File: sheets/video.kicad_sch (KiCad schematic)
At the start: 29 parts, among them U10 74LS273, U11 74LS05, U5 NEO-G0, U6 uPD4364CX-12, U7 uPD4364CX-12, U80 74HC04, U9 74LS273

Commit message: Adding Mouser Part Numbers
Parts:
- C67: Mouser (none) -> 810-FG28C0G1H221JNT0
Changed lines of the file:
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@@
+      (effects (font (size 1.27 1.27)) hide)
+    )
+    (property "Mouser" "" (at 238.506 146.558 0)
       (effects (font (size 1.27 1.27)) hide)
     )
@@
       (effects (font (size 1.27 1.27)) hide)
     )
+    (property "Mouser" "" (at 286.258 74.93 0)
+      (effects (font (size 1.27 1.27)) hide)
+    )
     (pin "1")
     (pin "2")
@@
       (effects (font (size 1.27 1.27)) hide)
     )
+    (property "Mouser" "" (at 286.258 121.158 0)
+      (effects (font (size 1.27 1.27)) hide)
+    )
     (pin "1")
     (pin "2")
@@
       (effects (font (size 1.27 1.27)) hide)
     )
+    (property "Mouser" "" (at 300.482 71.882 0)
+      (effects (font (size 1.27 1.27)) hide)
+    )
     (pin "1")
     (pin "2")
@@
       (effects (font (size 1.27 1.27)) hide)
     )
+    (property "Mouser" "" (at 286.258 50.546 0)
+      (effects (font (size 1.27 1.27)) hide)
+    )
     (pin "1")
     (pin "2")
@@
       (effects (font (size 1.27 1.27)) hide)
     )
+    (property "Mouser" "" (at 286.258 161.29 0)
+      (effects (font (size 1.27 1.27)) hide)
+    )
     (pin "1")
     (pin "2")
@@
     )
     (property "Datasheet" "" (at 282.194 177.038 0)
+      (effects (font (size 1.27 1.27)) hide)
+    )
+    (property "Mouser" "" (at 282.194 177.038 0)
       (effects (font (size 1.27 1.27)) hide)
     )
@@
       (effects (font (size 1.27 1.27)) hide)
     )
+    (property "Mouser" "" (at 293.37 82.042 0)
+      (effects (font (size 1.27 1.27)) hide)
+    )
     (pin "1")
     (pin "2")
@@
     )
     (property "Datasheet" "" (at 93.726 202.184 0)
+      (effects (font (size 1.27 1.27)) hide)
+    )
+    (property "Mouser" "" (at 93.726 202.184 0)
       (effects (font (size 1.27 1.27)) hide)
     )
@@
       (effects (font (size 1.27 1.27)) hide)
     )
+    (property "Mouser" "" (at 238.506 73.914 0)
+      (effects (font (size 1.27 1.27)) hide)
+    )
     (pin "1")
     (pin "10")
@@
       (effects (font (size 1.27 1.27)) hide)
     )
+    (property "Mouser" "" (at 286.258 62.738 0)
+      (effects (font (size 1.27 1.27)) hide)
+    )
     (pin "1")
     (pin "2")
@@
       (effects (font (size 1.27 1.27)) hide)
     )
+    (property "Mouser" "" (at 300.482 118.11 0)
+      (effects (font (size 1.27 1.27)) hide)
+    )
     (pin "1")
     (pin "2")
@@
       (effects (font (size 1.27 1.27)) hide)
     )
+    (property "Mouser" "" (at 286.258 143.002 0)
+      (effects (font (size 1.27 1.27)) hide)
+    )
     (pin "1")
     (pin "2")
@@
     )
     (property "Datasheet" "" (at 286.258 149.098 0)
+      (effects (font (size 1.27 1.27)) hide)
+    )
+    (property "Mouser" "" (at 286.258 149.098 0)
       (effects (font (size 1.27 1.27)) hide)
     )
@@
       (effects (font (size 1.27 1.27)) hide)
     )
+    (property "Mouser" "" (at 293.37 128.27 0)
+      (effects (font (size 1.27 1.27)) hide)
+    )
     (pin "1")
     (pin "2")
@@
     )
     (property "Datasheet" "" (at 177.038 120.65 0)
+      (effects (font (size 1.27 1.27)) hide)
+    )
+    (property "Mouser" "" (at 177.038 120.65 0)
       (effects (font (size 1.27 1.27)) hide)
     )
@@
     )
     (property "Datasheet" "" (at 139.7 214.884 0)
+      (effects (font (size 1.27 1.27)) hide)
+    )
+    (property "Mouser" "" (at 139.7 214.884 0)
       (effects (font (size 1.27 1.27)) hide)
     )
@@
       (effects (font (size 1.27 1.27)) hide)
     )
+    (property "Mouser" "" (at 177.038 66.294 0)
+      (effects (font (size 1.27 1.27)) hide)
+    )
     (pin "1")
     (pin "10")
@@
       (effects (font (size 1.27 1.27)) hide)
     )
+    (property "Mouser" "" (at 293.37 174.498 0)
+      (effects (font (size 1.27 1.27)) hide)
+    )
     (pin "1")
     (pin "2")
@@
     )
     (property "Datasheet" "" (at 286.258 96.774 0)
+      (effects (font (size 1.27 1.27)) hide)
+    )
+    (property "Mouser" "" (at 286.258 96.774 0)
       (effects (font (size 1.27 1.27)) hide)
     )
@@
       (effects (font (size 1.27 1.27)) hide)
     )
+    (property "Mouser" "810-FG28C0G1H221JNT0" (at 141.478 130.81 0)
+      (effects (font (size 1.27 1.27)) hide)
+    )
     (pin "1")
     (pin "2")
@@
     )
     (property "Datasheet" "" (at 259.842 213.36 0)
+      (effects (font (size 1.27 1.27)) hide)
+    )
+    (property "Mouser" "" (at 259.842 213.36 0)
       (effects (font (size 1.27 1.27)) hide)
     )
@@
       (effects (font (size 1.27 1.27)) hide)
     )
+    (property "Mouser" "" (at 286.258 115.062 0)
+      (effects (font (size 1.27 1.27)) hide)
+    )
     (pin "1")
     (pin "2")
@@
       (effects (font (size 1.27 1.27)) hide)
     )
+    (property "Mouser" "" (at 300.482 164.338 0)
+      (effects (font (size 1.27 1.27)) hide)
+    )
     (pin "1")
     (pin "2")
@@
     )
     (property "Datasheet" "" (at 286.258 167.386 0)
+      (effects (font (size 1.27 1.27)) hide)
+    )
+    (property "Mouser" "" (at 286.258 167.386 0)
       (effects (font (size 1.27 1.27)) hide)
     )
@@
     )
     (property "Datasheet" "" (at 69.342 202.184 0)
+      (effects (font (size 1.27 1.27)) hide)
+    )
+    (property "Mouser" "" (at 69.342 202.184 0)
       (effects (font (size 1.27 1.27)) hide)
     )
@@
       (effects (font (size 1.27 1.27)) hide)
     )
+    (property "Mouser" "" (at 282.194 130.81 0)
+      (effects (font (size 1.27 1.27)) hide)
+    )
     (pin "1")
     (pin "2")
@@
       (effects (font (size 1.27 1.27)) hide)
     )
+    (property "Mouser" "" (at 286.258 102.87 0)
+      (effects (font (size 1.27 1.27)) hide)
+    )
     (pin "1")
     (pin "2")
@@
     )
     (property "Datasheet" "" (at 272.796 83.312 0)
+      (effects (font (size 1.27 1.27)) hide)
+    )
+    (property "Mouser" "" (at 272.796 83.312 0)
       (effects (font (size 1.27 1.27)) hide)
     )
@@
       (effects (font (size 1.27 1.27)) hide)
     )
+    (property "Mouser" "" (at 286.258 68.834 0)
+      (effects (font (size 1.27 1.27)) hide)
+    )
     (pin "1")
     (pin "2")
@@
     )
     (property "Datasheet" "" (at 259.842 227.076 0)
+      (effects (font (size 1.27 1.27)) hide)
+    )
+    (property "Mouser" "" (at 259.842 227.076 0)
       (effects (font (size 1.27 1.27)) hide)
     )
@@
       (effects (font (size 1.27 1.27)) hide)
     )
+    (property "Mouser" "" (at 286.258 155.194 0)
+      (effects (font (size 1.27 1.27)) hide)
+    )
     (pin "1")
     (pin "2")
@@
       (effects (font (size 1.27 1.27)) hide)
     )
+    (property "Mouser" "" (at 286.258 56.642 0)
+      (effects (font (size 1.27 1.27)) hide)
+    )
     (pin "1")
     (pin "2")
@@
       (effects (font (size 1.27 1.27)) hide)
     )
+    (property "Mouser" "" (at 286.258 108.966 0)
+      (effects (font (size 1.27 1.27)) hide)
+    )
     (pin "1")
     (pin "2")
@@
       (effects (font (size 1.27 1.27)) hide)
     )
+    (property "Mouser" "" (at 259.842 199.644 0)
+      (effects (font (size 1.27 1.27)) hide)
+    )

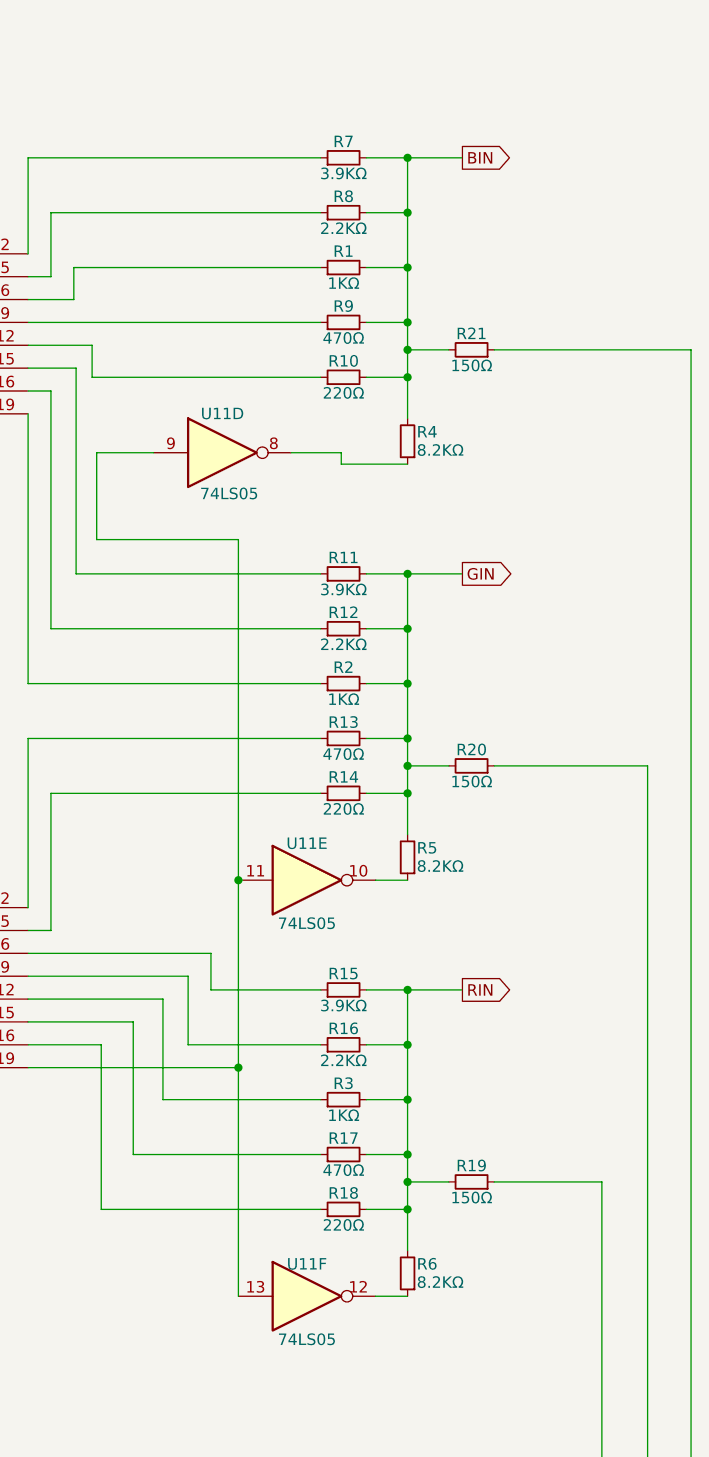
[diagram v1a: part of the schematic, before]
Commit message: More silkscreen tidy up, adding mouser components to BOM
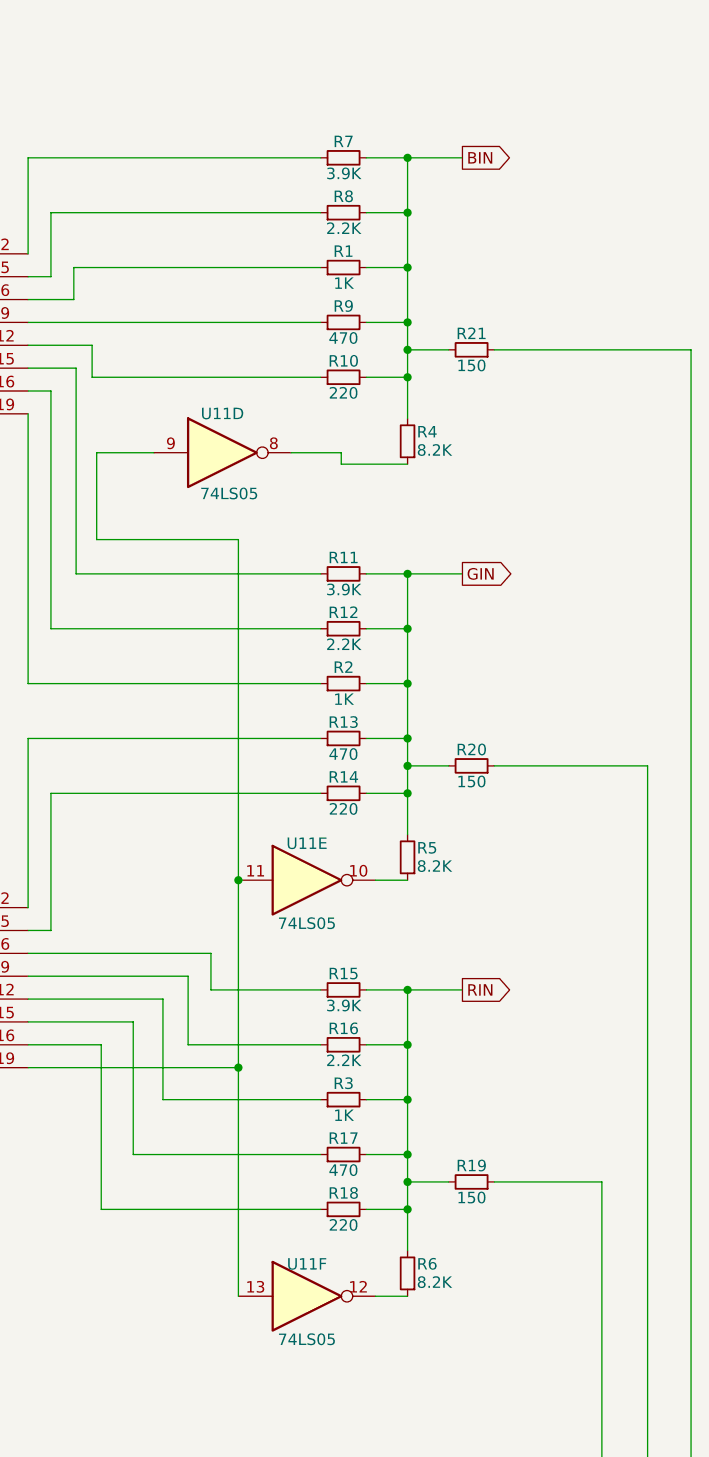
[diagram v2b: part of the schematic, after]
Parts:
- R1, R2, R3: value 1KΩ -> 1K
- R10, R14, R18: value 220Ω -> 220
- R11, R15, R7: value 3.9KΩ -> 3.9K
- R12, R16, R8: value 2.2KΩ -> 2.2K
- R13, R17, R9: value 470Ω -> 470
- R19, R20, R21: value 150Ω -> 150
- R4, R5, R6: value 8.2KΩ -> 8.2K
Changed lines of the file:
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@@
       (effects (font (size 1.27 1.27)))
     )
-    (property "Value" "220Ω" (at 286.258 76.708 90)
+    (property "Value" "220" (at 286.258 76.708 90)
       (effects (font (size 1.27 1.27)))
     )
@@
       (effects (font (size 1.27 1.27)))
     )
-    (property "Value" "220Ω" (at 286.258 122.936 90)
+    (property "Value" "220" (at 286.258 122.936 90)
       (effects (font (size 1.27 1.27)))
     )
@@
       (effects (font (size 1.27 1.27)))
     )
-    (property "Value" "150Ω" (at 300.482 73.66 90)
+    (property "Value" "150" (at 300.482 73.66 90)
       (effects (font (size 1.27 1.27)))
     )
@@
       (effects (font (size 1.27 1.27)))
     )
-    (property "Value" "3.9KΩ" (at 286.258 52.324 90)
+    (property "Value" "3.9K" (at 286.258 52.324 90)
       (effects (font (size 1.27 1.27)))
     )
@@
       (effects (font (size 1.27 1.27)))
     )
-    (property "Value" "470Ω" (at 286.258 163.068 90)
+    (property "Value" "470" (at 286.258 163.068 90)
       (effects (font (size 1.27 1.27)))
     )
@@
       (effects (font (size 1.27 1.27)) (justify right))
     )
-    (property "Value" "8.2KΩ" (at 294.386 83.058 0)
+    (property "Value" "8.2K" (at 294.386 83.058 0)
       (effects (font (size 1.27 1.27)) (justify right))
     )
@@
       (effects (font (size 1.27 1.27)))
     )
-    (property "Value" "1KΩ" (at 286.258 64.516 90)
+    (property "Value" "1K" (at 286.258 64.516 90)
       (effects (font (size 1.27 1.27)))
     )
@@
       (effects (font (size 1.27 1.27)))
     )
-    (property "Value" "150Ω" (at 300.482 119.888 90)
+    (property "Value" "150" (at 300.482 119.888 90)
       (effects (font (size 1.27 1.27)))
     )
@@
       (effects (font (size 1.27 1.27)))
     )
-    (property "Value" "3.9KΩ" (at 286.258 144.78 90)
+    (property "Value" "3.9K" (at 286.258 144.78 90)
       (effects (font (size 1.27 1.27)))
     )
@@
       (effects (font (size 1.27 1.27)))
     )
-    (property "Value" "2.2KΩ" (at 286.258 150.876 90)
+    (property "Value" "2.2K" (at 286.258 150.876 90)
       (effects (font (size 1.27 1.27)))
     )
@@
       (effects (font (size 1.27 1.27)) (justify right))
     )
-    (property "Value" "8.2KΩ" (at 294.386 129.286 0)
+    (property "Value" "8.2K" (at 294.386 129.286 0)
       (effects (font (size 1.27 1.27)) (justify right))
     )
@@
       (effects (font (size 1.27 1.27)) (justify right))
     )
-    (property "Value" "8.2KΩ" (at 294.386 175.514 0)
+    (property "Value" "8.2K" (at 294.386 175.514 0)
       (effects (font (size 1.27 1.27)) (justify right))
     )
@@
       (effects (font (size 1.27 1.27)))
     )
-    (property "Value" "3.9KΩ" (at 286.258 98.552 90)
+    (property "Value" "3.9K" (at 286.258 98.552 90)
       (effects (font (size 1.27 1.27)))
     )
@@
       (effects (font (size 1.27 1.27)))
     )
-    (property "Value" "470Ω" (at 286.258 116.84 90)
+    (property "Value" "470" (at 286.258 116.84 90)
       (effects (font (size 1.27 1.27)))
     )
@@
       (effects (font (size 1.27 1.27)))
     )
-    (property "Value" "150Ω" (at 300.482 166.116 90)
+    (property "Value" "150" (at 300.482 166.116 90)
       (effects (font (size 1.27 1.27)))
     )
@@
       (effects (font (size 1.27 1.27)))
     )
-    (property "Value" "220Ω" (at 286.258 169.164 90)
+    (property "Value" "220" (at 286.258 169.164 90)
       (effects (font (size 1.27 1.27)))
     )
@@
       (effects (font (size 1.27 1.27)))
     )
-    (property "Value" "2.2KΩ" (at 286.258 104.648 90)
+    (property "Value" "2.2K" (at 286.258 104.648 90)
       (effects (font (size 1.27 1.27)))
     )
@@
       (effects (font (size 1.27 1.27)))
     )
-    (property "Value" "470Ω" (at 286.258 70.612 90)
+    (property "Value" "470" (at 286.258 70.612 90)
       (effects (font (size 1.27 1.27)))
     )
@@
       (effects (font (size 1.27 1.27)))
     )
-    (property "Value" "1KΩ" (at 286.258 156.972 90)
+    (property "Value" "1K" (at 286.258 156.972 90)
       (effects (font (size 1.27 1.27)))
     )
@@
       (effects (font (size 1.27 1.27)))
     )
-    (property "Value" "2.2KΩ" (at 286.258 58.42 90)
+    (property "Value" "2.2K" (at 286.258 58.42 90)
       (effects (font (size 1.27 1.27)))
     )
@@
       (effects (font (size 1.27 1.27)))
     )
-    (property "Value" "1KΩ" (at 286.258 110.744 90)
-      (effects (font (size 1.27 1.27)))
-    )
+    (property "Value" "1K" (at 286.258 110.744 90)
+      (effects (font (size 1.27 1.27)))
+    )

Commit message: Little tweaks to silkscreen Updated BOM with mouser parts
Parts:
- R1, R2, R3: Mouser (none) -> 71-CMF501K0000FHEA
- R10, R14, R18: Mouser (none) -> 71-RN60D2200F
- R11, R15, R7: Mouser (none) -> 71-RN60D3901F
- R12, R16, R8: Mouser (none) -> 71-RN60D2201F
- R13, R17, R9: Mouser (none) -> 71-RN60C4700F
- R19, R20, R21: Mouser (none) -> 71-RN60E1500F
- R4, R5, R6: Mouser (none) -> 71-RN60D-F-8.2K
- U10, U9: Mouser (none) -> 595-SN74LS273N
- U11: Mouser (none) -> 595-SN74LS05N
- U5, U6, U7: Comment (none) -> Use Original
- U80: Mouser (none) -> 595-SN74HC04N

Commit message: update before public
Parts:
- R1, R2, R3: Mouser 71-CMF501K0000FHEA -> (none)
- R10, R14, R18: Mouser 71-RN60D2200F -> (none)
- R11, R15, R7: Mouser 71-RN60D3901F -> (none)
- R12, R16, R8: Mouser 71-RN60D2201F -> (none)
- R13, R17, R9: Mouser 71-RN60C4700F -> (none)
- R19, R20, R21: Mouser 71-RN60E1500F -> (none)
- R4, R5, R6: Mouser 71-RN60D-F-8.2K -> (none)

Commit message: Tweaks to BOM
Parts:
- R1, R2, R3: Mouser (none) -> 71-CMF501K0000FHEA
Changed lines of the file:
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@@
       (effects (font (size 1.27 1.27)) hide)
     )
-    (property "Mouser" "" (at 286.258 62.738 0)
+    (property "Mouser" "71-CMF501K0000FHEA" (at 286.258 62.738 0)
       (effects (font (size 1.27 1.27)) hide)
     )
@@
       (effects (font (size 1.27 1.27)) hide)
     )
-    (property "Mouser" "" (at 286.258 155.194 0)
+    (property "Mouser" "71-CMF501K0000FHEA" (at 286.258 155.194 0)
       (effects (font (size 1.27 1.27)) hide)
     )
@@
       (effects (font (size 1.27 1.27)) hide)
     )
-    (property "Mouser" "" (at 286.258 108.966 0)
-      (effects (font (size 1.27 1.27)) hide)
-    )
+    (property "Mouser" "71-CMF501K0000FHEA" (at 286.258 108.966 0)
+      (effects (font (size 1.27 1.27)) hide)
+    )
